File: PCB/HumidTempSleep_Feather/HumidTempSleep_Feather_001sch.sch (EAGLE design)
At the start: 3 parts

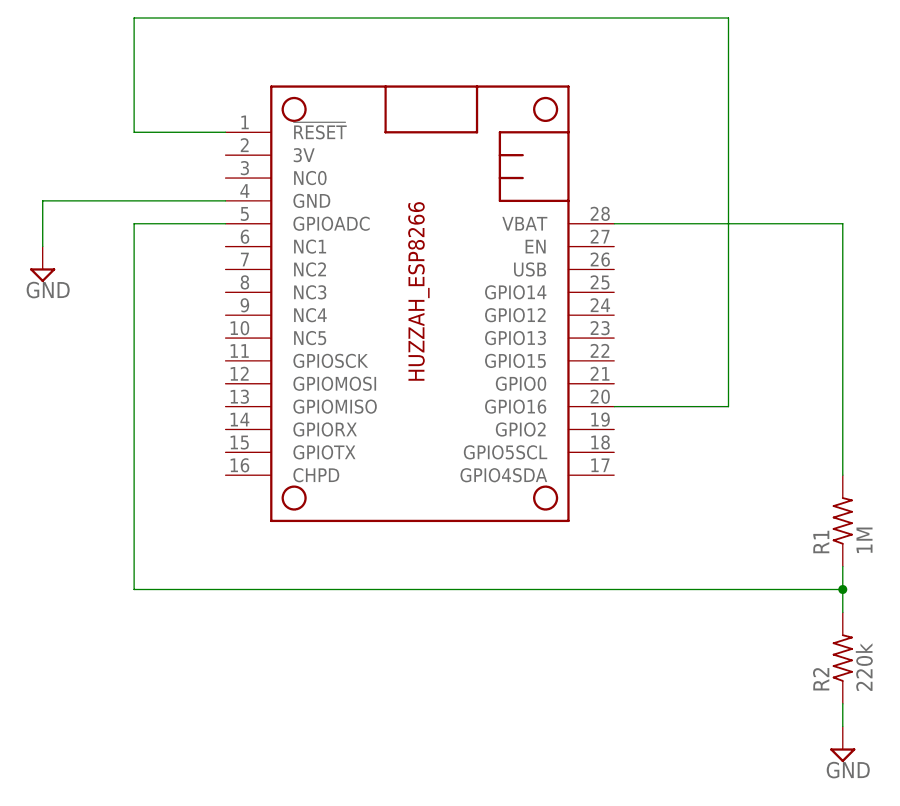
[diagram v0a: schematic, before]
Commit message: Added some jumpers
Added the jumpers for turning off the reset and the batery monitoring.
Also put on some jumpers to parallel the connections to the Feather.
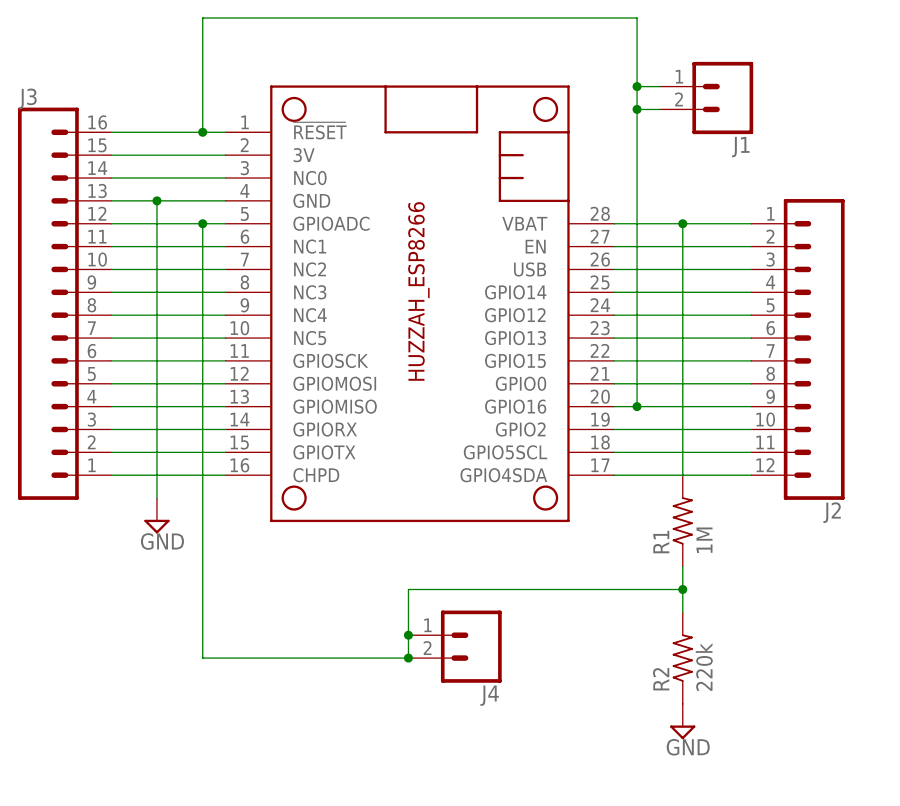
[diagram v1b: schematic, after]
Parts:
- added J1, J4: (no value), SparkFun-Connectors:CONN_02
- added J2: (no value), SparkFun-Connectors:CONN_12
- added J3: (no value), SparkFun-Connectors:CONN_16
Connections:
- removed net N$3: MS2.GPIOADC, R1.1, R2.2
- new net 3V: J3.15, MS2.3V
- new net N$10: J2.11, MS2.GPIO5SCL
- new net N$11: J2.12, MS2.GPIO4SDA
- new net N$12: J3.14, MS2.NC0
- new net N$13: J3.11, MS2.NC1
- new net N$14: J3.10, MS2.NC2
- new net N$15: J3.9, MS2.NC3
- new net N$16: J3.8, MS2.NC4
- new net N$17: J3.7, MS2.NC5
- new net N$18: J3.6, MS2.GPIOSCK
- new net N$19: J3.5, MS2.GPIOMOSI
- new net N$2: J2.2, MS2.EN
- new net N$20: J3.4, MS2.GPIOMISO
- new net N$21: J3.3, MS2.GPIORX
- new net N$22: J3.2, MS2.GPIOTX
- new net N$23: J3.1, MS2.CHPD
- new net N$24: J3.12, J4.1, J4.2, MS2.GPIOADC, R1.1, R2.2
- new net N$4: J2.4, MS2.GPIO14
- new net N$5: J2.5, MS2.GPIO12
- new net N$6: J2.6, MS2.GPIO13
- new net N$7: J2.7, MS2.GPIO15
- new net N$8: J2.8, MS2.GPIO0
- new net N$9: J2.10, MS2.GPIO2
- new net USB: J2.3, MS2.USB
- net GND: now also J3.13
- net N$1: now also J1.1, J1.2, J2.9, J3.16
- net VBAT: now also J2.1
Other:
- moved on the sheet: R1, R2
